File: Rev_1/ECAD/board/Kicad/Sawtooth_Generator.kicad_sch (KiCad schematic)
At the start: 8 parts, among them Q201 PNP, U201 NE555D

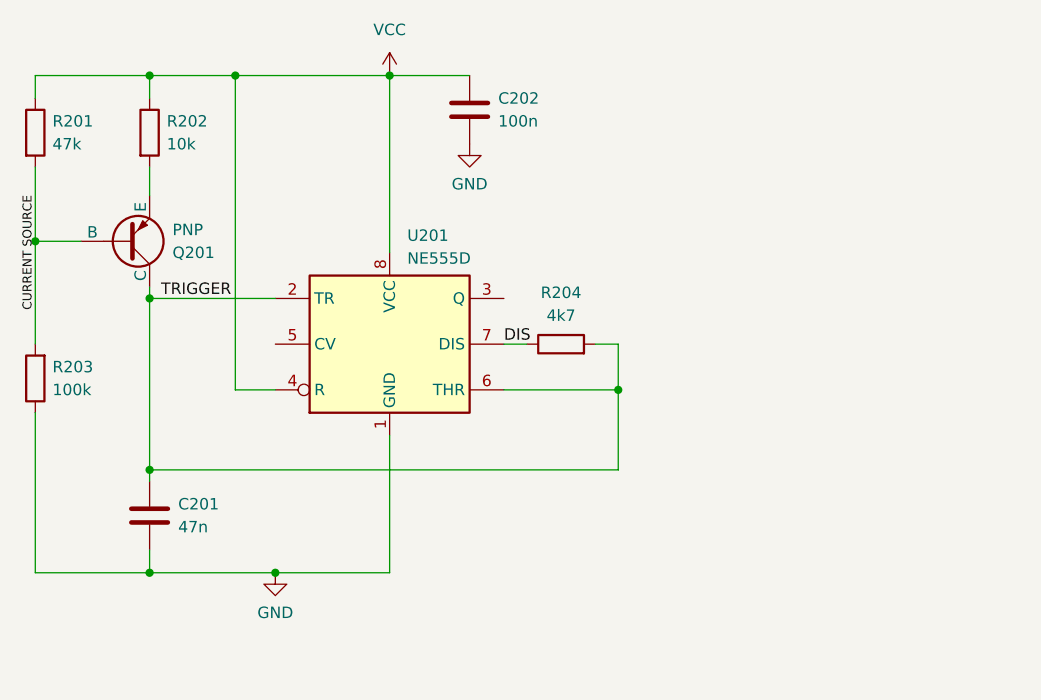
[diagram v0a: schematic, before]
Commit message: Added filter hierarchy
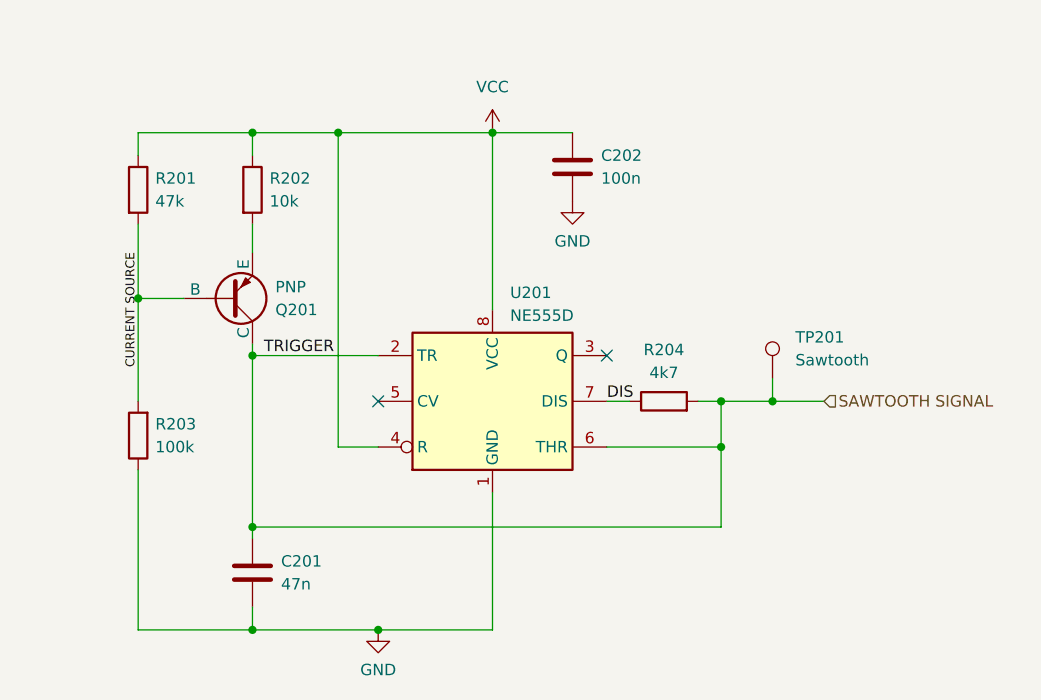
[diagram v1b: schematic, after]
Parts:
- added TP201: Sawtooth, symbol Connector:TestPoint
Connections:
- net TRIGGER renamed SAWTOOTH SIGNAL
- net SAWTOOTH SIGNAL: now also TP201.1
- no-connect marks 0 -> 2
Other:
- moved on the sheet: C201, C202, Q201, R201, R202, R203, R204, U201
